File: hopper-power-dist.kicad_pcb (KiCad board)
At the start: 2 copper layers, 109 x 79 mm, 34 parts, among them J1 XT90PW-M, J2 B2B-XH-A(LF)(SN), J3 XT60PW-F, J4 XT60PW-F, J5 XT60PW-F, J6 XT60PW-F, J7 XT60PW-F, J8 B2B-XH-A(LF)(SN), SW2 FT_Power_Switch

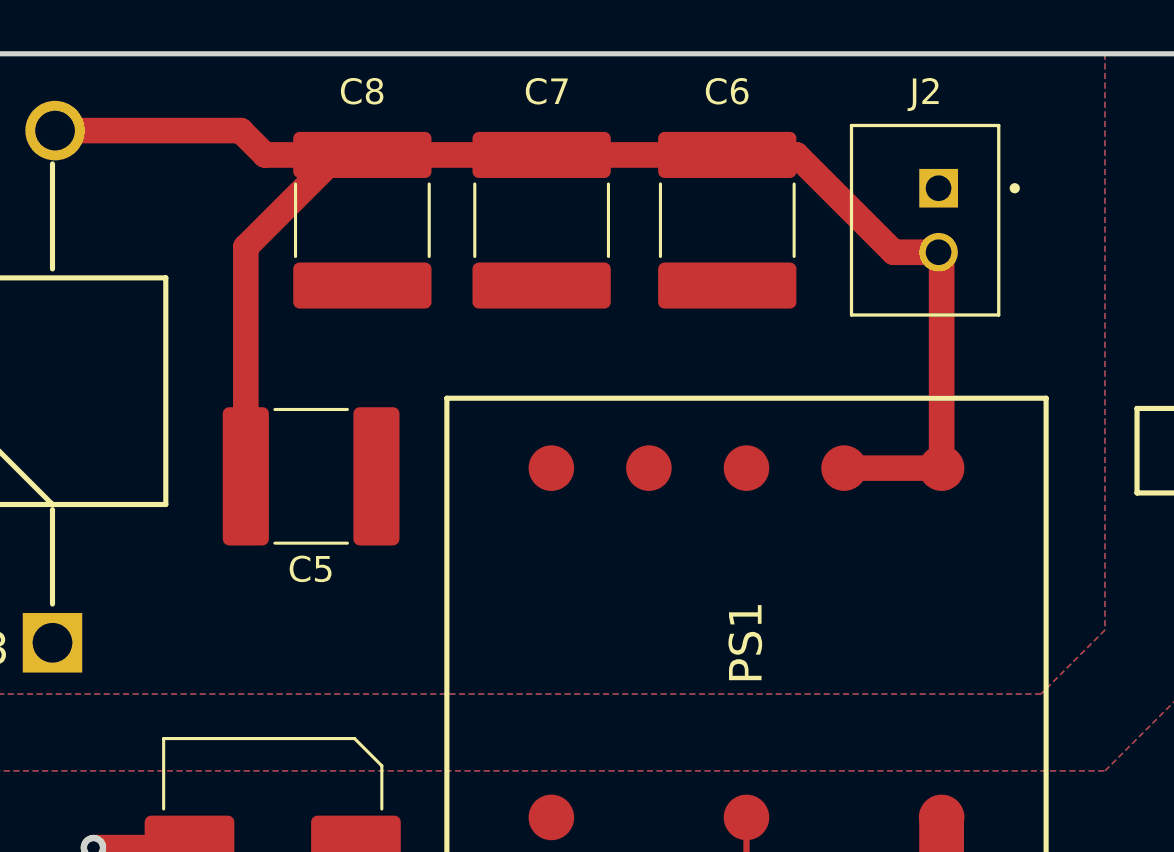
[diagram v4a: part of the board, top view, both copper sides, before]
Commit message: Moved BEC JST connector to be more accessible
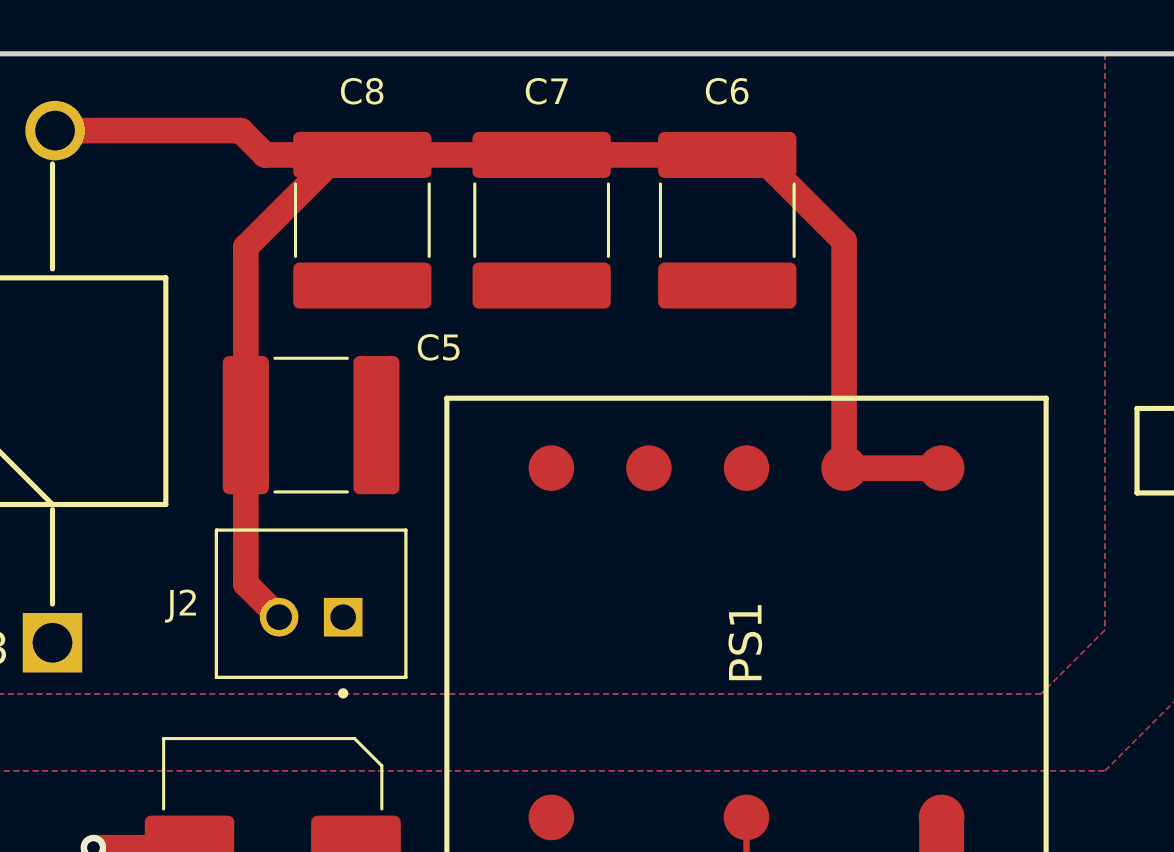
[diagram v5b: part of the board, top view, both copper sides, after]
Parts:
- moved J2 29.0 mm to (99.0, 85.0), turned to 0 degrees
- moved C5 2.00 mm to (99.0, 77.5)
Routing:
- net /-12V: track 63.7 -> 68.3 mm
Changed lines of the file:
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@@
   )
   (footprint "B2B-XH-A_LF__SN_:JST_B2B-XH-A(LF)(SN)" (layer "F.Cu")
-    (at 123.5 69.5 90)
+    (at 99 85)
     (property "AVAILABILITY" "In Stock")
     (property "DESCRIPTION" "Connector Header Through Hole 2 position 0.098 (2.50mm)")
@@
     (property "Sheetname" "")
     (attr through_hole)
-    (fp_text reference "J2" (at 5 -0.5 180) (layer "F.SilkS")
-      (effects (font (size 1 1) (thickness 0.15)))
-    )
-    (fp_text value "B2B-XH-A(LF)(SN)" (at 8.75 4.11 90) (layer "F.Fab")
+    (fp_text reference "J2" (at -5 -0.525 180) (layer "F.SilkS")
+      (effects (font (size 1 1) (thickness 0.15)))
+    )
+    (fp_text value "B2B-XH-A(LF)(SN)" (at 8.75 4.11) (layer "F.Fab")
       (effects (font (size 1 1) (thickness 0.15)))
     )
@@
     (fp_line (start -3.7 2.35) (end -3.7 -3.4) (layer "F.Fab") (width 0.127))
     (fp_circle (center 1.25 2.975) (end 1.35 2.975) (layer "F.Fab") (width 0.2) (fill none))
-    (pad "1" thru_hole rect locked (at 1.25 0 90) (size 1.508 1.508) (drill 1) (layers *.Cu *.Mask)
+    (pad "1" thru_hole rect locked (at 1.25 0) (size 1.508 1.508) (drill 1) (layers *.Cu *.Mask)
       (net 10 "Net-(C5-Pad1)") (pinfunction "1") (pintype "passive"))
-    (pad "2" thru_hole circle locked (at -1.25 0 90) (size 1.508 1.508) (drill 1) (layers *.Cu *.Mask)
+    (pad "2" thru_hole circle locked (at -1.25 0) (size 1.508 1.508) (drill 1) (layers *.Cu *.Mask)
       (net 3 "/-12V") (pinfunction "2") (pintype "passive"))
+    (model "D:/Documents/KiCad/6.0/footprints/B2B-XH-A_LF__SN_.pretty/B2B-XH-A_LF__SN_.step"
+      (offset (xyz 0 0.5 0))
+      (scale (xyz 1 1 1))
+      (rotate (xyz -90 0 0))
+    )
   )
   (footprint "MountingHole:MountingHole_2.2mm_M2" locked (layer "F.Cu")
@@
   )
   (footprint "Capacitor_SMD:C_2220_5650Metric" (layer "F.Cu")
-    (at 99 79.5 180)
+    (at 99 77.5 180)
     (descr "Capacitor SMD 2220 (5650 Metric), square (rectangular) end terminal, IPC_7351 nominal, (Body size from: http://datasheets.avx.com/AVX-HV_MLCC.pdf), generated with kicad-footprint-generator")
     (tags "capacitor")
@@
     (property "Sheetname" "")
     (attr smd)
-    (fp_text reference "C5" (at 0 -3.65) (layer "F.SilkS")
+    (fp_text reference "C5" (at -5 3) (layer "F.SilkS")
       (effects (font (size 1 1) (thickness 0.15)))
     )
@@
     (pad "2" thru_hole circle locked (at -1.25 0 180) (size 1.508 1.508) (drill 1) (layers *.Cu *.Mask)
       (net 6 "Net-(J1-PadP)") (pinfunction "2") (pintype "passive"))
+    (model "D:/Documents/KiCad/6.0/footprints/B2B-XH-A_LF__SN_.pretty/B2B-XH-A_LF__SN_.step"
+      (offset (xyz 0 0.5 0))
+      (scale (xyz 1 1 1))
+      (rotate (xyz -90 0 0))
+    )
   )
   (gr_rect locked (start 55 63) (end 164 142) (layer "Edge.Cuts") (width 0.2) (fill none))
@@
   (via (at 100.5 111.5) (size 0.8) (drill 0.4) (layers "F.Cu" "B.Cu") (free) (net 2))
   (via (at 90.5 94) (size 1) (drill 0.5) (layers "F.Cu" "B.Cu") (free) (net 2))
-  (segment (start 123.5 70.75) (end 121.75 70.75) (width 1) (layer "F.Cu") (net 3))
   (segment (start 96.45 70.55) (end 100.05 66.95) (width 1) (layer "F.Cu") (net 3))
-  (segment (start 123.62 79.18) (end 123.62 70.87) (width 1) (layer "F.Cu") (net 3))
+  (segment (start 119.81 79.18) (end 119.81 70.31) (width 1) (layer "F.Cu") (net 3))
+  (segment (start 96.45 77.5) (end 96.45 83.7) (width 1) (layer "F.Cu") (net 3))
   (segment (start 108 66.95) (end 101 66.95) (width 1) (layer "F.Cu") (net 3))
   (segment (start 97.2 66.95) (end 96.25 66) (width 1) (layer "F.Cu") (net 3))
-  (segment (start 121.75 70.75) (end 117.95 66.95) (width 1) (layer "F.Cu") (net 3))
+  (segment (start 96.45 83.7) (end 97.75 85) (width 1) (layer "F.Cu") (net 3))
   (segment (start 101 66.95) (end 97.2 66.95) (width 1) (layer "F.Cu") (net 3))
   (segment (start 119.81 79.18) (end 123.62 79.18) (width 1) (layer "F.Cu") (net 3))
+  (segment (start 116.45 66.95) (end 115.25 66.95) (width 1) (layer "F.Cu") (net 3))
   (segment (start 100.05 66.95) (end 101 66.95) (width 1) (layer "F.Cu") (net 3))
-  (segment (start 117.95 66.95) (end 115.25 66.95) (width 1) (layer "F.Cu") (net 3))
-  (segment (start 123.62 70.87) (end 123.5 70.75) (width 1) (layer "F.Cu") (net 3))
+  (segment (start 119.81 70.31) (end 116.45 66.95) (width 1) (layer "F.Cu") (net 3))
   (segment (start 96.45 79.5) (end 96.45 70.55) (width 1) (layer "F.Cu") (net 3))
   (segment (start 96.25 66) (end 89 66) (width 1) (layer "F.Cu") (net 3))
@@
   (segment (start 125 103.5) (end 131.0425 103.5) (width 0.25) (layer "F.Cu") (net 8))
   (segment (start 116 94.5) (end 125 103.5) (width 0.25) (layer "F.Cu") (net 8))
-  (segment (start 101.87 79.18) (end 101.55 79.5) (width 1) (layer "F.Cu") (net 10))
   (zone (net 10) (net_name "Net-(C5-Pad1)") (layer "F.Cu") (hatch edge 0.508)
     (connect_pads (clearance 0.508))

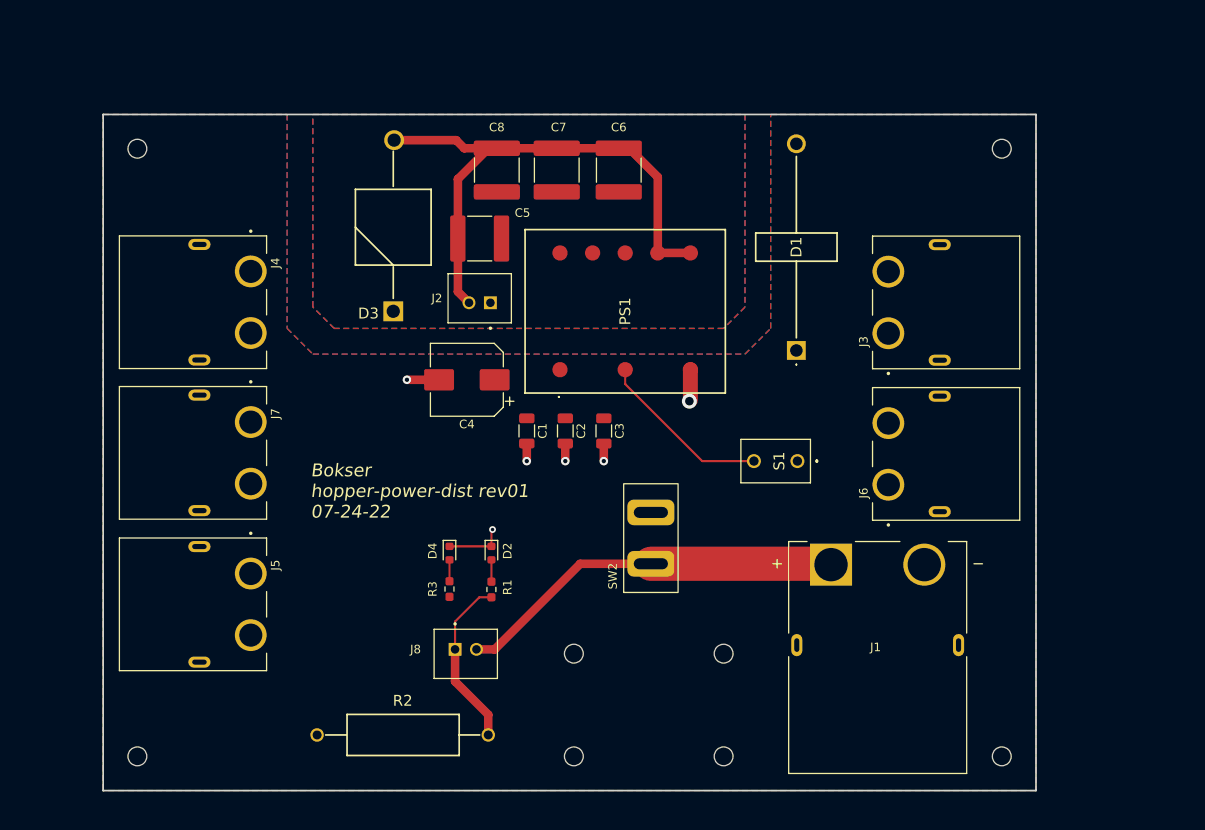
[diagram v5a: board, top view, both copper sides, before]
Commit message: Start rev02, fix minor mistakes and add xt60pw-m series
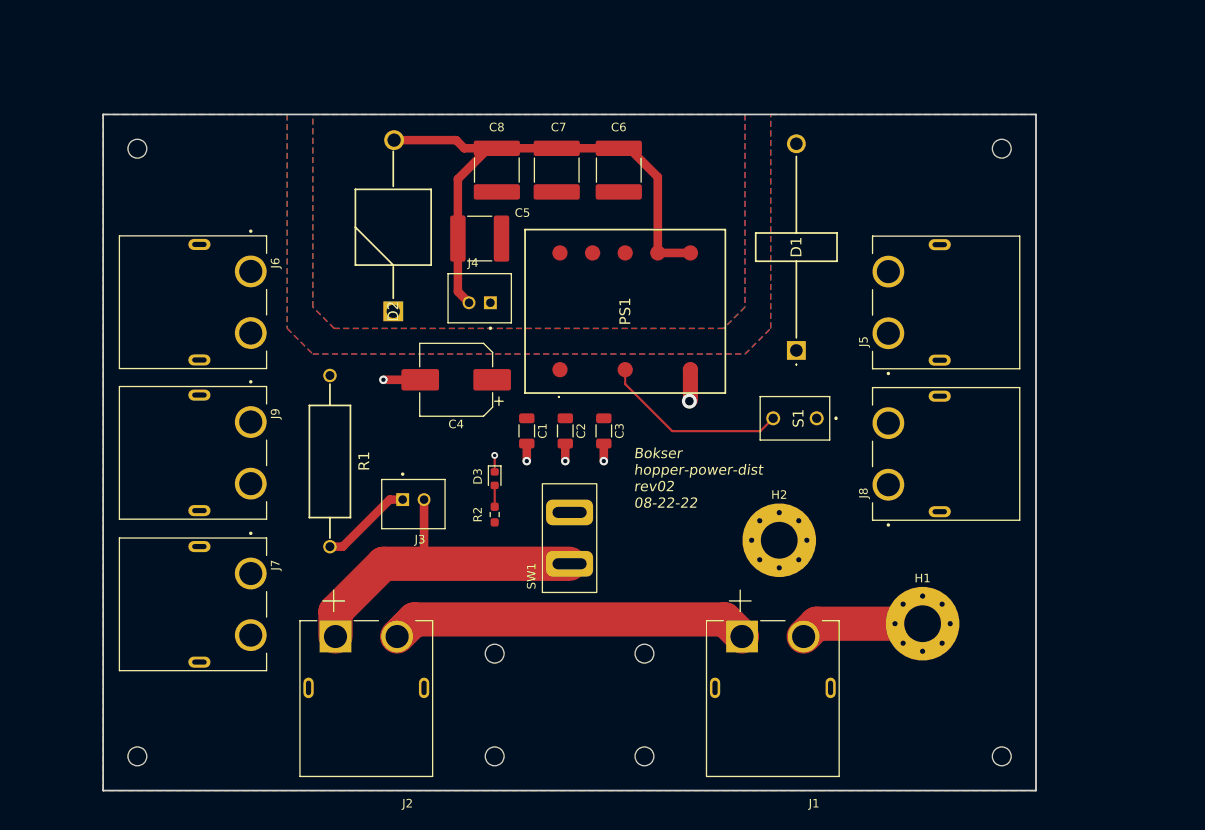
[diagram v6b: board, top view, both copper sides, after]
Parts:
- removed the D2 at (100.4, 114.2)
- removed the R1 at (100.4, 118.5)
- added H1: B-, MountingHole:MountingHole_4.3mm_M4_Pad_Via, F.Cu at (150.8, 122.5)
- added H2: C-, MountingHole:MountingHole_4.3mm_M4_Pad_Via, F.Cu at (134.0, 112.8)
- added J2: XT60PW-M, XT60PW-F:AMASS_XT60PW-M, F.Cu at (85.8, 130.0)
- C4: footprint Capacitor_SMD:CP_Elec_8x10 -> benbokser:CP_Elec_8x10_MAL214699903E3
- J1: value XT90PW-M -> XT60PW-M; footprint XT90PW-M:AMASS_XT90PW-M -> XT60PW-F:AMASS_XT60PW-M
- moved R1 28.7 mm to (81.5, 113.5), turned to 90 degrees
- moved J3 18.5 mm to (91.2, 108.0)
- moved J1 13.2 mm to (133.2, 130.0), turned to 180 degrees
- moved D3 10.2 mm to (100.8, 105.5)
- moved R2 10.2 mm to (100.8, 109.8)
- moved SW1 9.50 mm to (109.5, 112.5)
- moved REF 9.25 mm to (118.2, 138.0)
- moved REF** 9.25 mm to (100.8, 138.0)
- moved REF** 9.25 mm to (100.8, 126.0)
- moved REF** 9.25 mm to (118.2, 126.0)
- moved S1 5.48 mm to (138.4, 98.5)
- moved C4 1.25 mm to (96.2, 94.0)
- renumbered D3 to D2, D4 to D3, J8 to J3, J2 to J4, J3 to J5, J4 to J6, J5 to J7, J6 to J8, J7 to J9, R2 to R1, R3 to R2, SW2 to SW1
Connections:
- J3 pad 2: Net-(J1-PadP) -> Net-(J2-Pad1)
- J5 pad S1: GND -> unconnected-(J5-PadS1)
- J5 pad S2: GND -> unconnected-(J5-PadS2)
- J6 pad S1: GND -> unconnected-(J6-PadS1)
- J6 pad S2: GND -> unconnected-(J6-PadS2)
- J7 pad S1: GND -> unconnected-(J7-PadS1)
- J7 pad S2: GND -> unconnected-(J7-PadS2)
- J8 pad S1: GND -> unconnected-(J8-PadS1)
- J8 pad S2: GND -> unconnected-(J8-PadS2)
- J9 pad S1: GND -> unconnected-(J9-PadS1)
- J9 pad S2: GND -> unconnected-(J9-PadS2)
- SW1 pad 1: Net-(J1-PadP) -> Net-(J2-Pad1)
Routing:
- net Net-(J1-PadP): track 45.5 -> 0.00 mm
- net Net-(J1-Pad1): track 0.00 -> 42.0 mm
- net Net-(J2-Pad1): track 0.00 -> 40.4 mm
- net Net-(H1-Pad1): track 0.00 -> 14.5 mm
- net Net-(J3-Pad1): track 20.3 -> 10.8 mm
- net GND: track 20.5 -> 16.4 mm
- net Net-(D2-Pad2): track 2.55 -> 0.00 mm
- net Net-(PS1-Pad2): track 20.5 -> 21.9 mm
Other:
- board text added: "Bokser hopper-power-dist rev02 08-22-22"
- board text removed: "Bokser hopper-power-dist rev01 07-24-22"

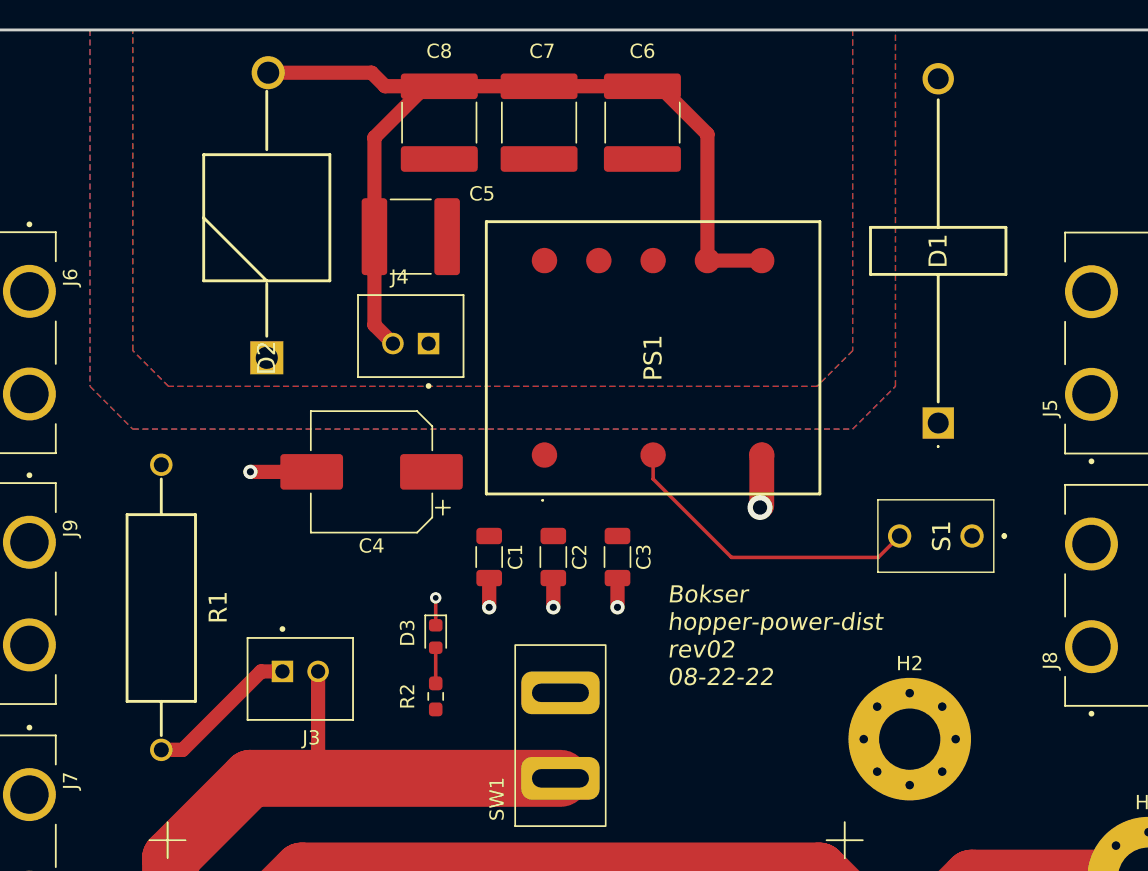
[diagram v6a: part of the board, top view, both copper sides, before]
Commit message: Replace DC-DC converter with thru-hole version and clean up
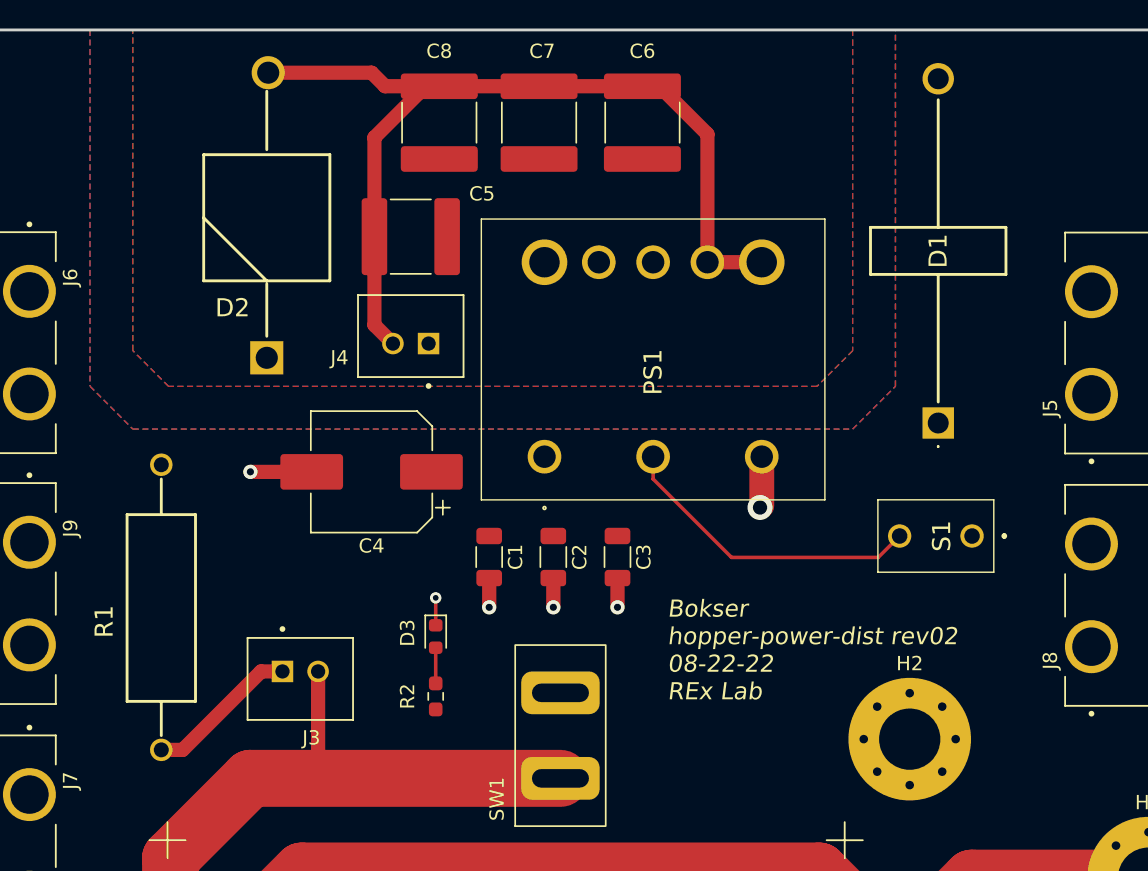
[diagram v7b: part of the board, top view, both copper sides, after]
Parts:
- PS1: footprint SamacSys_Parts:ULT1225D48NMC -> SamacSys_Parts:ULT1225D48NC
- moved PS1 10.3 mm to (108.4, 92.9)
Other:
- board text added: "Bokser hopper-power-dist rev02 08-22-22 REx Lab"
- board text removed: "Bokser hopper-power-dist rev02 08-22-22"
